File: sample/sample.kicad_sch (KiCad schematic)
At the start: 93 parts, among them M1 PMOS4pin, M10 NMOS3pin_1, M11 PMOS3pin_1, M12 NMOS3pin_2, M13 PMOS3pin_2, M14 NMOS4pin, M15 PMOS4pin, M2 PMOS4pin, M3 PMOS4pin, M4 NMOS4pin, M5 NMOS4pin, M6 NMOS4pin, M7 NMOS4pin, M8 NMOS4pin, M9 NMOS3pin_1, Q1 NPN, Q2 PNP, SW1 SW_CMOS, SW2 SW_SPDT, SW3 SW_SPST_OFF, SW4 SW_SPST_ON, U1 V_{DD}, U10 D_FF_R, U11 or31, U12 D_FF_R, U13 D_FF_R, U14 not, U15 nor21, U16 nor21, U17 GND_Drafting, U18 GND_Drafting, U19 GND_Drafting, U2 V_{DD}, U20 GND_Drafting, U21 OP_AMP, U24 RS_FF, U25 OP_AMP, U26 nand21, U27 nor21, U28 RS_FF, U29 JK_FF, U3 V_{DD}, U30 MUX21, U31 OP_AMP, U32 nand31, U33 nor31, U35 Differential_AMP, U36 and21, U37 or21, U38 D_FF, U39 T_FF, U4 V_{DD}, U40 MUX31, U41 and31, U42 or31, U43 Differential_AMP, U44 D_FF_R, U45 not, U46 xnor21, U47 MUX41, U48 VDD_Drafting, U49 buf, U5 V_{DD}, U50 xnor31, U51 GND_Drafting, U52 D_FF_R_S, U53 xor21, U54 xor31, U6 nand21, U7 delay, U8 D_FF_R, U9 D_FF_R

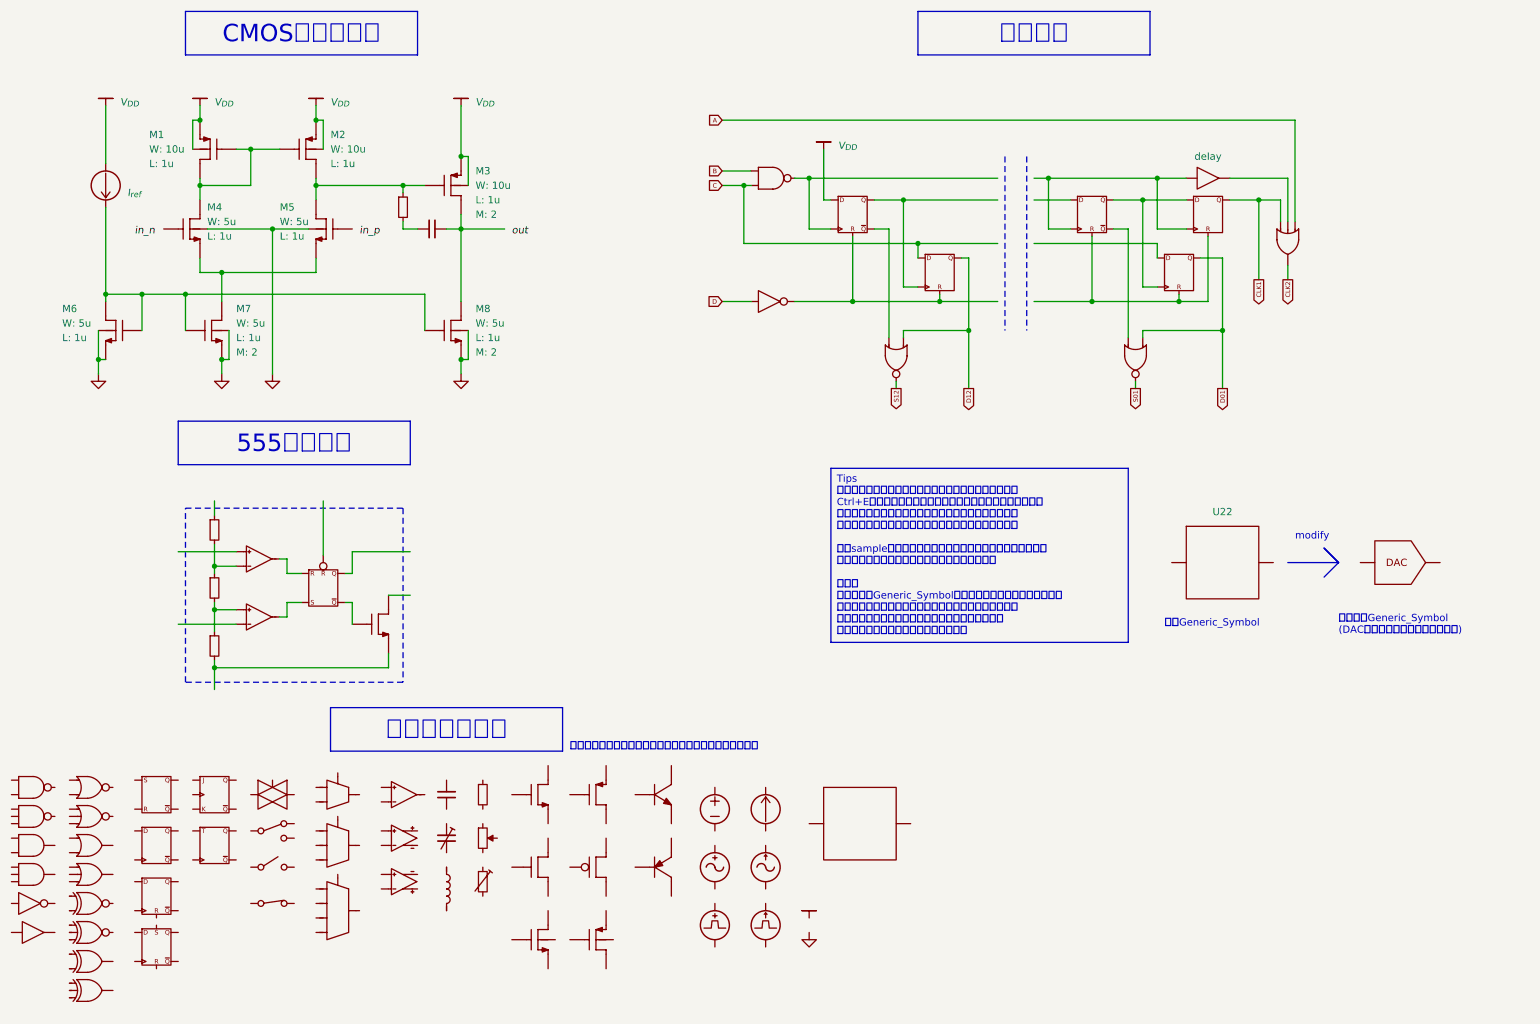
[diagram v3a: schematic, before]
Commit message: MOSとBJTのシンボルを変更
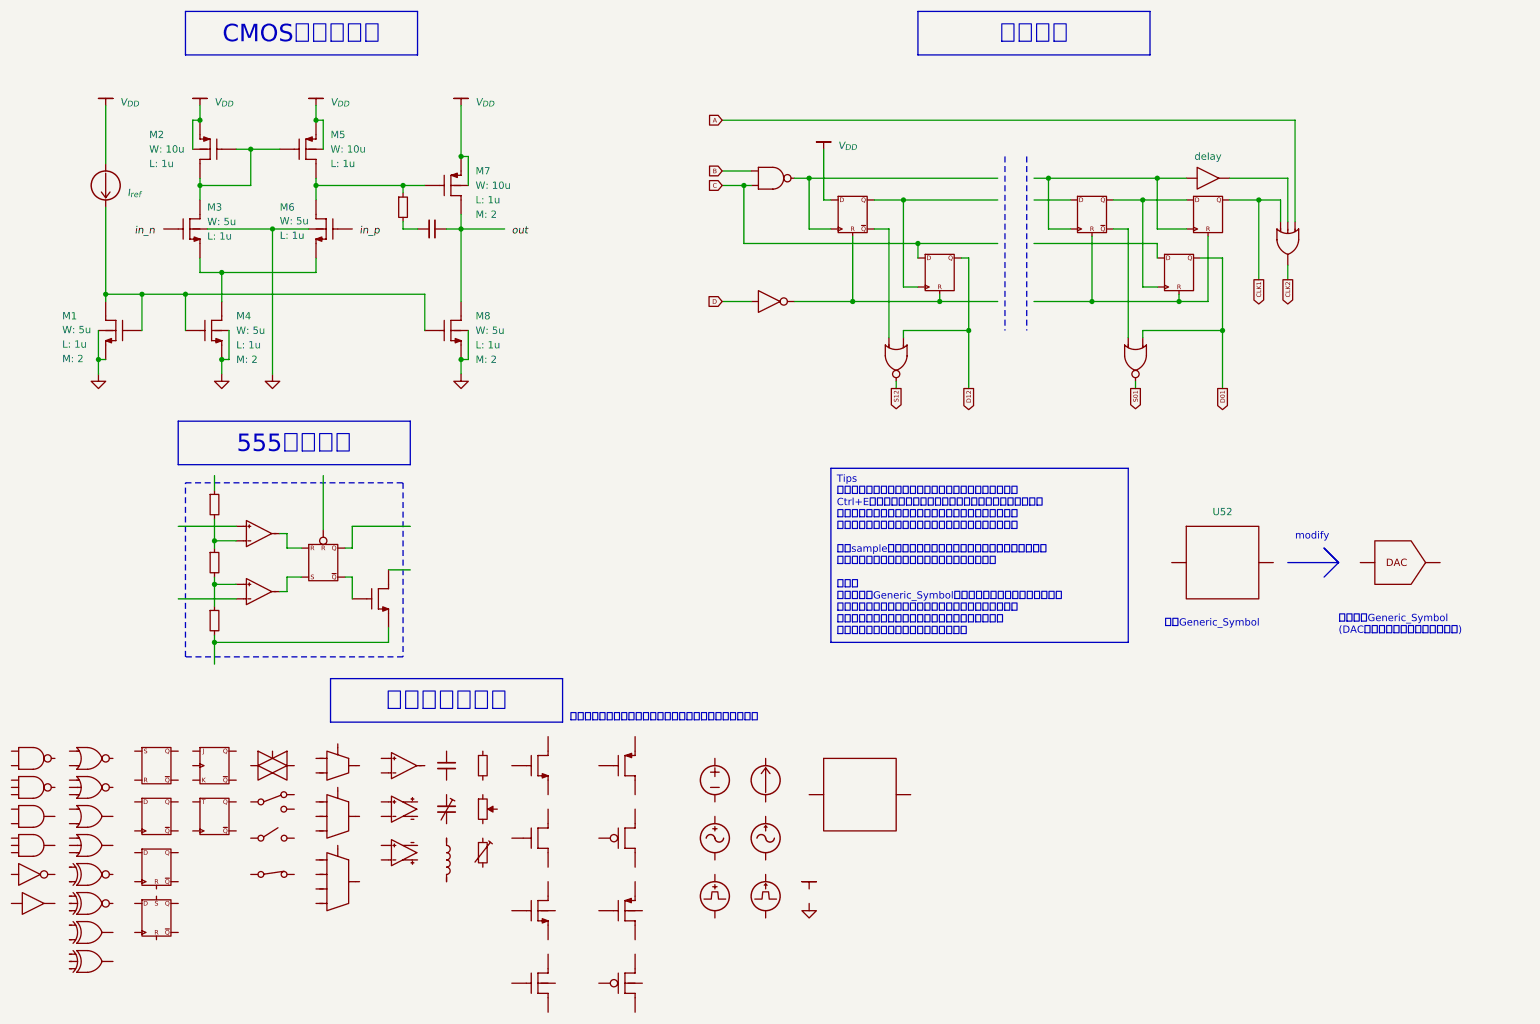
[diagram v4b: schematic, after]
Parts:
- removed M1, M15, M2, M3: PMOS4pin, symbol Drafting_Symbols:PMOS4pin
- removed M11: PMOS3pin_1, symbol Drafting_Symbols:PMOS3pin_1
- removed M12: NMOS3pin_2, symbol Drafting_Symbols:NMOS3pin_2
- removed M13: PMOS3pin_2, symbol Drafting_Symbols:PMOS3pin_2
- removed M14, M4, M5, M6, M7, M8: NMOS4pin, symbol Drafting_Symbols:NMOS4pin
- removed Q1: NPN, symbol Drafting_Symbols:NPN
- removed Q2: PNP, symbol Drafting_Symbols:PNP
- added M1, M12, M3, M4, M6, M8: NMOS4pin_1, symbol Drafting_Symbols:NMOS4pin_1
- added M11: NMOS3pin_2, symbol Drafting_Symbols:NMOS3pin_2
- added M13: NMOS4pin, symbol Drafting_Symbols:NMOS4pin_2
- added M14: PMOS3pin_1, symbol Drafting_Symbols:PMOS3pin_1
- added M15: PMOS3pin_2, symbol Drafting_Symbols:PMOS3pin_2
- added M16, M2, M5, M7: PMOS4pin_1, symbol Drafting_Symbols:PMOS4pin_1
- added M17: PMOS4pin, symbol Drafting_Symbols:PMOS4pin_2
- renumbered R2 to R1, R3 to R2, R4 to R3, R1 to R4, U26 to U1, U42 to U10, U46 to U11, U50 to U12, U53 to U13, U54 to U14, U17 to U15, U1 to U16, U28 to U17, U38 to U18, U44 to U19, U32 to U2, U52 to U20, U2 to U21, U29 to U22, U39 to U23, U18 to U24, U21 to U25, U25 to U26, U19 to U27, U3 to U28, U24 to U29, U36 to U3, U40 to U31, U47 to U32, U31 to U33, U35 to U34, U43 to U35, U4 to U36, U20 to U37, U6 to U38, U14 to U39, U41 to U4, U48 to U40, U51 to U41, U5 to U42, U8 to U43, U34 to U44, U15 to U45, U12 to U46, U9 to U47, U16 to U48, U13 to U49, U45 to U5, U7 to U50, U10 to U51, U22 to U52, U11 to U53, U23 to U54, U49 to U6, U27 to U7, U33 to U8, U37 to U9
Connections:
- net GND: now also M1.3 (S), M1.4 (B), M2.2 (S), M2.4 (B), M3.4 (B), M4.3 (S), M4.4 (B), M5.2 (S), M5.4 (B), M6.4 (B), M7.2 (S), M7.4 (B), M8.3 (S), M8.4 (B)
- net at R4.1: now also M5.3 (D), M6.2 (D), M7.1 (G)
- net at U29.1 (~Q): now also M9.1 (S)
- net at U26.1 (out): no longer U29.1 (~Q)
- net at U25.1 (out): no longer U29.1 (~Q)
- net at M9.1 (S): no longer U29.1 (~Q)
- net at C1.2: now also M7.3 (D), M8.2 (D)
- net at U50.1 (Y): now also U47.1 (~Q), U51.1 (R); no longer U53.1 (Y)
- net at I_DC1.1: now also M1.1 (G), M1.2 (D), M4.1 (G), M8.1 (G)
- net at U47.1 (~Q): now also U49.1 (R), U51.1 (R)
- new net: U26.1 (out), U29.1 (~Q)
- new net: U25.1 (out), U29.1 (~Q)
- new net: U38.1 (Y), U43.1 (~Q)
- new net: M3.3 (S), M4.2 (D), M6.3 (S)
- new net: M2.1 (G), M2.3 (D), M3.2 (D), M5.1 (G)
- new net: U43.1 (~Q), U45.1 (Y)
- new net: U50.1 (Y), U53.1 (Y)
- new net: U39.1 (Y), U43.1 (~Q), U46.1 (R)
- new net: U47.1 (~Q), U48.1 (Y)
- new net: U47.1 (~Q), U49.1 (R), U51.1 (R)
- new net: U43.1 (~Q), U46.1 (R)

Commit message: サンプルの修正
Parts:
- added Q1: NPN, symbol Drafting_Symbols:NPN
- added Q2: PNP, symbol Drafting_Symbols:PNP
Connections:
- net at U29.1 (~Q): now also M9.1 (S)
- net at U26.1 (out): no longer U29.1 (~Q)
- net at U25.1 (out): no longer U29.1 (~Q)
- net at M9.1 (S): no longer U29.1 (~Q)
- net at U50.1 (Y): now also U47.1 (~Q), U51.1 (R); no longer U53.1 (Y)
- net at U47.1 (~Q): now also U49.1 (R), U51.1 (R)
- new net: U26.1 (out), U29.1 (~Q)
- new net: U25.1 (out), U29.1 (~Q)
- new net: U38.1 (Y), U43.1 (~Q)
- new net: U43.1 (~Q), U45.1 (Y)
- new net: U50.1 (Y), U53.1 (Y)
- new net: U39.1 (Y), U43.1 (~Q), U46.1 (R)
- new net: U47.1 (~Q), U48.1 (Y)
- new net: U47.1 (~Q), U49.1 (R), U51.1 (R)
- new net: U43.1 (~Q), U46.1 (R)
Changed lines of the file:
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@@
 	)
 	(symbol
-		(lib_name "Drafting_Symbols:Generic_Symbol")
 		(lib_id "Drafting_Symbols:Generic_Symbol")
 		(at 165.1 157.48 0)
@@
 	)
 	(symbol
-		(lib_name "Drafting_Symbols:OP_AMP")
 		(lib_id "Drafting_Symbols:OP_AMP")
 		(at 59.69 121.92 0)
@@
 	)
 	(symbol
-		(lib_name "Drafting_Symbols:nor21")
 		(lib_id "Drafting_Symbols:nor21")
 		(at 171.45 81.28 270)
@@
 	)
 	(symbol
-		(lib_name "Drafting_Symbols:Generic_Symbol")
 		(lib_id "Drafting_Symbols:Generic_Symbol")
 		(at 228.6 116.84 0)
@@
 	)
 	(symbol
-		(lib_name "Drafting_Symbols:OP_AMP")
 		(lib_id "Drafting_Symbols:OP_AMP")
 		(at 59.69 111.76 0)
@@
 	)
 	(symbol
-		(lib_name "Drafting_Symbols:nor21")
 		(lib_id "Drafting_Symbols:nor21")
 		(at 213.36 81.28 270)
@@
 	)
 	(symbol
+		(lib_id "Drafting_Symbols:NPN")
+		(at 139.7 190.5 0)
+		(unit 1)
+		(exclude_from_sim no)
+		(in_bom yes)
+		(on_board yes)
+		(dnp no)
+		(fields_autoplaced yes)
+		(property "Reference" "Q1"
+			(at 140.97 190.4999 0)
+			(effects
+				(font
+					(size 1.27 1.27)
+				)
+				(justify left)
+				(hide yes)
+			)
+		)
+		(property "Value" "NPN"
+			(at 138.43 184.15 0)
+			(effects
+				(font
+					(size 1.27 1.27)
+				)
+				(hide yes)
+			)
+		)
+		(property "Footprint" ""
+			(at 138.43 184.15 0)
+			(effects
+				(font
+					(size 1.27 1.27)
+				)
+				(hide yes)
+			)
+		)
+		(property "Datasheet" ""
+			(at 138.43 184.15 0)
+			(effects
+				(font
+					(size 1.27 1.27)
+				)
+				(hide yes)
+			)
+		)
+		(property "Description" ""
+			(at 139.7 190.5 0)
+			(effects
+				(font
+					(size 1.27 1.27)
+				)
+				(hide yes)
+			)
+		)
+		(pin "3"
+		)
+		(pin "2"
+		)
+		(pin "1"
+		)
+		(instances
+			(project ""
+				(path "/95969ed8-3a0e-4f54-b05c-15f0e2c163e6"
+					(reference "Q1")
+					(unit 1)
+				)
+			)
+		)
+	)
+	(symbol
 		(lib_name "D_FF_R_3")
 		(lib_id "Drafting_Symbols:D_FF_R")
@@
 					(unit 1)
 				)
+			)
+		)
+	)
+	(symbol
+		(lib_id "Drafting_Symbols:PNP")
+		(at 148.59 190.5 0)
+		(unit 1)
+		(exclude_from_sim no)
+		(in_bom yes)
+		(on_board yes)
+		(dnp no)
+		(fields_autoplaced yes)
+		(property "Reference" "Q2"
+			(at 149.86 190.4999 0)
+			(effects
+				(font
+					(size 1.27 1.27)
+				)
+				(justify left)
+				(hide yes)
+			)
+		)
+		(property "Value" "PNP"
+			(at 147.32 184.15 0)
+			(effects
+				(font
+					(size 1.27 1.27)
+				)
+				(hide yes)
+			)
+		)
+		(property "Footprint" ""
+			(at 147.32 184.15 0)
+			(effects
+				(font
+					(size 1.27 1.27)
+				)
+				(hide yes)
+			)
+		)
+		(property "Datasheet" ""
+			(at 147.32 184.15 0)
+			(effects
+				(font
+					(size 1.27 1.27)
+				)
+				(hide yes)
+			)
+		)
+		(property "Description" ""
+			(at 148.59 190.5 0)
+			(effects
+				(font
+					(size 1.27 1.27)
+				)
+				(hide yes)
+			)
+		)
+		(pin "1"
+		)
+		(pin "3"
+		)
+		(pin "2"
+		)
+		(instances
+			(project ""
+				(path "/95969ed8-3a0e-4f54-b05c-15f0e2c163e6"
+					(reference "Q2")
+					(unit 1)
+				)

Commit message: KiCad9対応
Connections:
- net at U29.1 (~Q): now also M9.1 (S)
- net at U26.1 (out): no longer U29.1 (~Q)
- net at U25.1 (out): no longer U29.1 (~Q)
- net at M9.1 (S): no longer U29.1 (~Q)
- net at U50.1 (Y): now also U47.1 (~Q), U51.1 (Q); no longer U53.1 (Y)
- net at U47.1 (~Q): now also U49.1 (Q), U51.1 (Q)
- new net: U26.1 (out), U29.1 (~Q)
- new net: U25.1 (out), U29.1 (~Q)
- new net: U38.1 (Y), U43.1 (~Q)
- new net: U43.1 (~Q), U45.1 (Y)
- new net: U50.1 (Y), U53.1 (Y)
- new net: U39.1 (Y), U43.1 (~Q), U46.1 (Q)
- new net: U47.1 (~Q), U48.1 (Y)
- new net: U47.1 (~Q), U49.1 (Q), U51.1 (Q)
- new net: U43.1 (~Q), U46.1 (Q)
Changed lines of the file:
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@@
 (kicad_sch
-	(version 20231120)
+	(version 20250114)
 	(generator "eeschema")
-	(generator_version "8.0")
+	(generator_version "9.0")
 	(paper "A4")
 	(title_block
@@
 		(rev "v1.0")
 	)
+	(rectangle
+		(start 46.99 102.87)
+		(end 85.09 133.35)
+		(stroke
+			(width 0.2)
+			(type dot)
+		)
+		(fill
+			(type none)
+		)
+	)
+	(text "元のGeneric_Symbol"
+		(exclude_from_sim no)
+		(at 218.44 128.27 0)
+		(effects
+			(font
+				(size 1.27 1.27)
+			)
+			(justify left bottom)
+		)
+	)
+	(text "modify"
+		(exclude_from_sim no)
+		(at 241.3 113.03 0)
+		(effects
+			(font
+				(size 1.27 1.27)
+			)
+			(justify left bottom)
+		)
+	)
+	(text "最新版のシンボルはここに含まれていないことがあります"
+		(exclude_from_sim no)
+		(at 114.3 144.78 0)
+		(effects
+			(font
+				(size 1.27 1.27)
+			)
+			(justify left bottom)
+		)
+	)
+	(text "変更後のGeneric_Symbol\n(DACのシンボルに作り変えている)"
+		(exclude_from_sim no)
+		(at 248.92 129.54 0)
+		(effects
+			(font
+				(size 1.27 1.27)
+			)
+			(justify left bottom)
+		)
+	)
+	(text_box "論理回路"
+		(exclude_from_sim no)
+		(at 175.26 20.32 0)
+		(size 40.64 7.62)
+		(margins 2.286 2.286 2.286 2.286)
+		(stroke
+			(width 0)
+			(type solid)
+		)
+		(fill
+			(type none)
+		)
+		(effects
+			(font
+				(size 3.048 3.048)
+			)
+		)
+	)
+	(text_box "Tips\n元あるシンボルと少しだけ違う物を使いたいときには、\nCtrl+Eで選択されたシンボルのみ変更することができます。\n回路図内のシンボルのみ変更され、元のライブラリ内の\nシンボルは変更されないので積極的に使うと便利です。\n\nこのsample内では、いくつかのシンボルにこの手法を使って\n入出力ピンを増やしたり減らしたりしています。\n\n応用編\nシンボル「Generic_Symbol」はほしいシンボルを作るときの\nひな形です。必要な形に作り変えて、入出力ピンを定義\nすることで任意のシンボルにすることができます。\n右に例を示すので参考にしてください。"
+		(exclude_from_sim no)
+		(at 160.02 100.33 0)
+		(size 52.07 30.48)
+		(margins 0.9525 0.9525 0.9525 0.9525)
+		(stroke
+			(width 0)
+			(type default)
+		)
+		(fill
+			(type none)
+		)
+		(effects
+			(font
+				(size 1.27 1.27)
+			)
+			(justify left top)
+		)
+	)
+	(text_box "全シンボル一覧"
+		(exclude_from_sim no)
+		(at 72.39 137.16 0)
+		(size 40.64 7.62)
+		(margins 2.286 2.286 2.286 2.286)
+		(stroke
+			(width 0)
+			(type solid)
+		)
+		(fill
+			(type none)
+		)
+		(effects
+			(font
+				(size 3.048 3.048)
+			)
+		)
+	)
+	(text_box "CMOSオペアンプ"
+		(exclude_from_sim no)
+		(at 46.99 20.32 0)
+		(size 40.64 7.62)
+		(margins 2.286 2.286 2.286 2.286)
+		(stroke
+			(width 0)
+			(type solid)
+		)
+		(fill
+			(type none)
+		)
+		(effects
+			(font
+				(size 3.048 3.048)
+			)
+		)
+	)
+	(text_box "555タイマー"
+		(exclude_from_sim no)
+		(at 45.72 92.075 0)
+		(size 40.64 7.62)
+		(margins 2.286 2.286 2.286 2.286)
+		(stroke
+			(width 0)
+			(type solid)
+		)
+		(fill
+			(type none)
+		)
+		(effects
+			(font
+				(size 3.048 3.048)
+			)
+		)
+	)
 	(junction
 		(at 69.85 50.8)
@@
 		)
 	)
-	(rectangle
-		(start 46.99 102.87)
-		(end 85.09 133.35)
-		(stroke
-			(width 0.2)
-			(type dot)
-		)
-		(fill
-			(type none)
-		)
-	)
-	(text_box "論理回路"
-		(exclude_from_sim no)
-		(at 175.26 20.32 0)
-		(size 40.64 7.62)
-		(stroke
-			(width 0)
-			(type solid)
-		)
-		(fill
-			(type none)
-		)
-		(effects
-			(font
-				(size 3.048 3.048)
-			)
-		)
-	)
-	(text_box "Tips\n元あるシンボルと少しだけ違う物を使いたいときには、\nCtrl+Eで選択されたシンボルのみ変更することができます。\n回路図内のシンボルのみ変更され、元のライブラリ内の\nシンボルは変更されないので積極的に使うと便利です。\n\nこのsample内では、いくつかのシンボルにこの手法を使って\n入出力ピンを増やしたり減らしたりしています。\n\n応用編\nシンボル「Generic_Symbol」はほしいシンボルを作るときの\nひな形です。必要な形に作り変えて、入出力ピンを定義\nすることで任意のシンボルにすることができます。\n右に例を示すので参考にしてください。"
-		(exclude_from_sim no)
-		(at 160.02 100.33 0)
-		(size 52.07 30.48)
-		(stroke
-			(width 0)
-			(type default)
-		)
-		(fill
-			(type none)
-		)
-		(effects
-			(font
-				(size 1.27 1.27)
-			)
-			(justify left top)
-		)
-	)
-	(text_box "全シンボル一覧"
-		(exclude_from_sim no)
-		(at 72.39 137.16 0)
-		(size 40.64 7.62)
-		(stroke
-			(width 0)
-			(type solid)
-		)
-		(fill
-			(type none)
-		)
-		(effects
-			(font
-				(size 3.048 3.048)
-			)
-		)
-	)
-	(text_box "CMOSオペアンプ"
-		(exclude_from_sim no)
-		(at 46.99 20.32 0)
-		(size 40.64 7.62)
-		(stroke
-			(width 0)
-			(type solid)
-		)
-		(fill
-			(type none)
-		)
-		(effects
-			(font
-				(size 3.048 3.048)
-			)
-		)
-	)
-	(text_box "555タイマー"
-		(exclude_from_sim no)
-		(at 45.72 92.075 0)
-		(size 40.64 7.62)
-		(stroke
-			(width 0)
-			(type solid)
-		)
-		(fill
-			(type none)
-		)
-		(effects
-			(font
-				(size 3.048 3.048)
-			)
-		)
-	)
-	(text "元のGeneric_Symbol"
-		(exclude_from_sim no)
-		(at 218.44 128.27 0)
-		(effects
-			(font
-				(size 1.27 1.27)
-			)
-			(justify left bottom)
-		)
-	)
-	(text "modify"
-		(exclude_from_sim no)
-		(at 241.3 113.03 0)
-		(effects
-			(font
-				(size 1.27 1.27)
-			)
-			(justify left bottom)
-		)
-	)
-	(text "最新版のシンボルはここに含まれていないことがあります"
-		(exclude_from_sim no)
-		(at 114.3 144.78 0)
-		(effects
-			(font
-				(size 1.27 1.27)
-			)
-			(justify left bottom)
-		)
-	)
-	(text "変更後のGeneric_Symbol\n(DACのシンボルに作り変えている)"
-		(exclude_from_sim no)
-		(at 248.92 129.54 0)
-		(effects
-			(font
-				(size 1.27 1.27)
-			)
-			(justify left bottom)
-		)
-	)
 	(label "in_n"
 		(at 38.1 59.69 0)
-		(fields_autoplaced yes)
 		(effects
 			(font
@@
 	(label "in_p"
 		(at 77.47 59.69 0)
-		(fields_autoplaced yes)
 		(effects
 			(font
@@
 	(label "out"
 		(at 104.14 59.69 0)
-		(fields_autoplaced yes)
 		(effects
 			(font
@@
 		)
 	)
+	(embedded_fonts no)
 )

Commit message: KiCad10対応
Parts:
- U44, U52, U54: value ~ -> (none)
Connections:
- net at U29.1 (~Q): now also M9.1 (S)
- net at U26.1 (out): no longer U29.1 (~Q)
- net at U25.1 (out): no longer U29.1 (~Q)
- net at M9.1 (S): no longer U29.1 (~Q)
- net at U50.1 (Y): now also U47.1 (~Q), U51.1 (Q); no longer U53.1 (Y)
- net at U47.1 (~Q): now also U49.1 (Q), U51.1 (Q)
- new net: U26.1 (out), U29.1 (~Q)
- new net: U25.1 (out), U29.1 (~Q)
- new net: U38.1 (Y), U43.1 (~Q)
- new net: U43.1 (~Q), U45.1 (Y)
- new net: U50.1 (Y), U53.1 (Y)
- new net: U39.1 (Y), U43.1 (~Q), U46.1 (Q)
- new net: U47.1 (~Q), U48.1 (Y)
- new net: U47.1 (~Q), U49.1 (Q), U51.1 (Q)
- new net: U43.1 (~Q), U46.1 (Q)
